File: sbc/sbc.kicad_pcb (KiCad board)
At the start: 4 copper layers, 101.6 x 101.6 mm, 72 parts, among them J1 Controller-Connector, J2 Controller-Connector, J3 SIO-Header, J4 QTPY-RP2040, J5 AVD-Header, J6 AVA-Header, J7 AudioOut-Connector, J8 VideoOut-Connector, J9 Power-Connector, U1 Sally, U10 AT27C256R, U11 AS6C4008-55SIN, U12 TXU0104, U13 TXU0204, U14 AP22814AW5, U2 Antic, U3 GTIA, U4 Pokey, U5 PIA, U6 74AHCT1G125GV,125, U7 74AHCT1G125GV,125, U8 AMU, U9 RMU, X1 3.579545 MHz

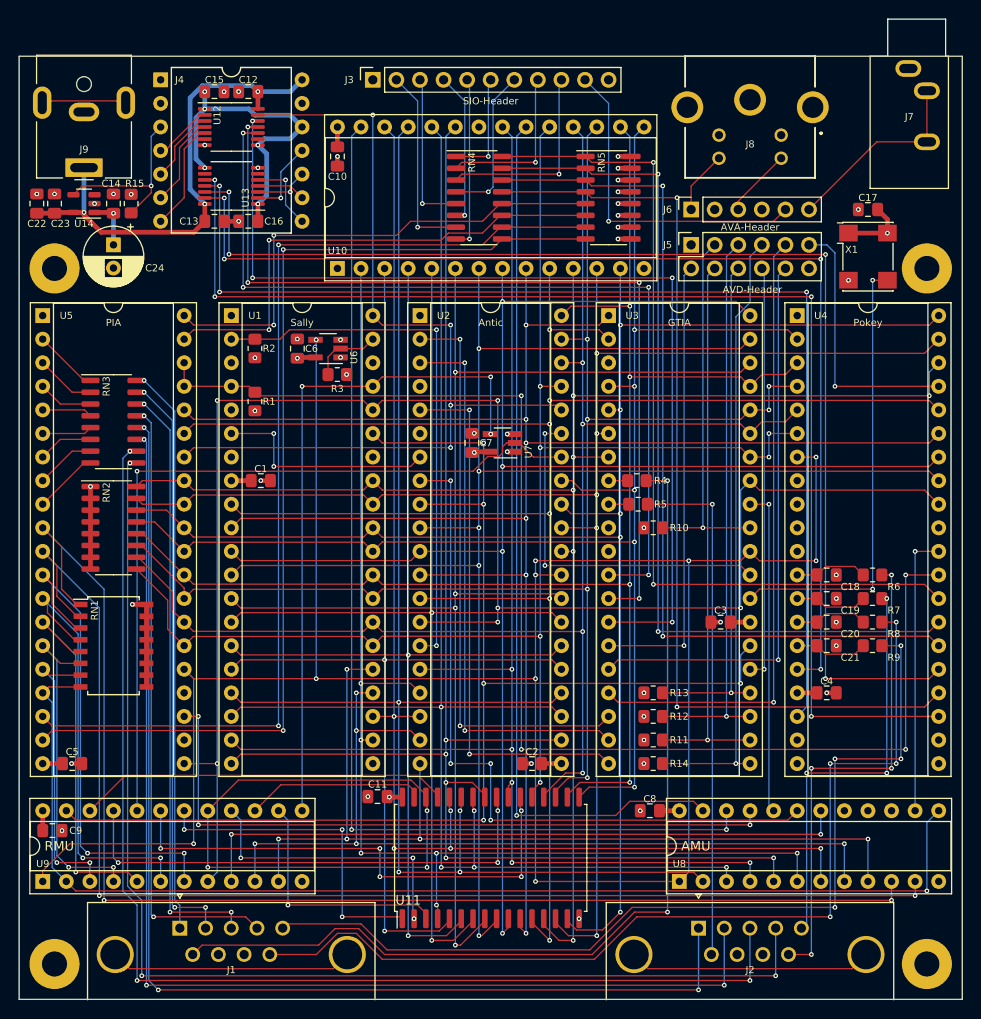
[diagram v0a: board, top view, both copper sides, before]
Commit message: SBC v1.2
SBC fixes/changes:

  - S-Video:
    - Fix S-Video footprint (Y and C swapped, and GNDs swapped) and adapt schematic to match
    - Wire S-Video grounds to AVA header instead of directly to (digital) GND
  - Audio:
    - Wire Audio-Out ground to AVA header
    - Drop SIO audio
    - Pullup open drain pokey audio
  - AMU/RMU:
    - Connect ROM and RAM OE to GND
    - Reserve AMU pin for "IO"
    - Reserve RMU pin for "antic" (registered halt)
    - Support for separate Antic banking (clock RMU with /phi2)
    - Supoprt 130XE and 320XE (compy)
  - Add the option for a resistor between OSC, PHI0 buffer and PHI2 buffer (to reduce over/under-shoot)
  - Invert CA2 (a PNP transistor on the Atari 800 XL inverts this signal)

Additions:

  - SBC Audio/Video board
  - SBC Case
  - SBC SD board

Stylize the complete system as "SFF 320XE".
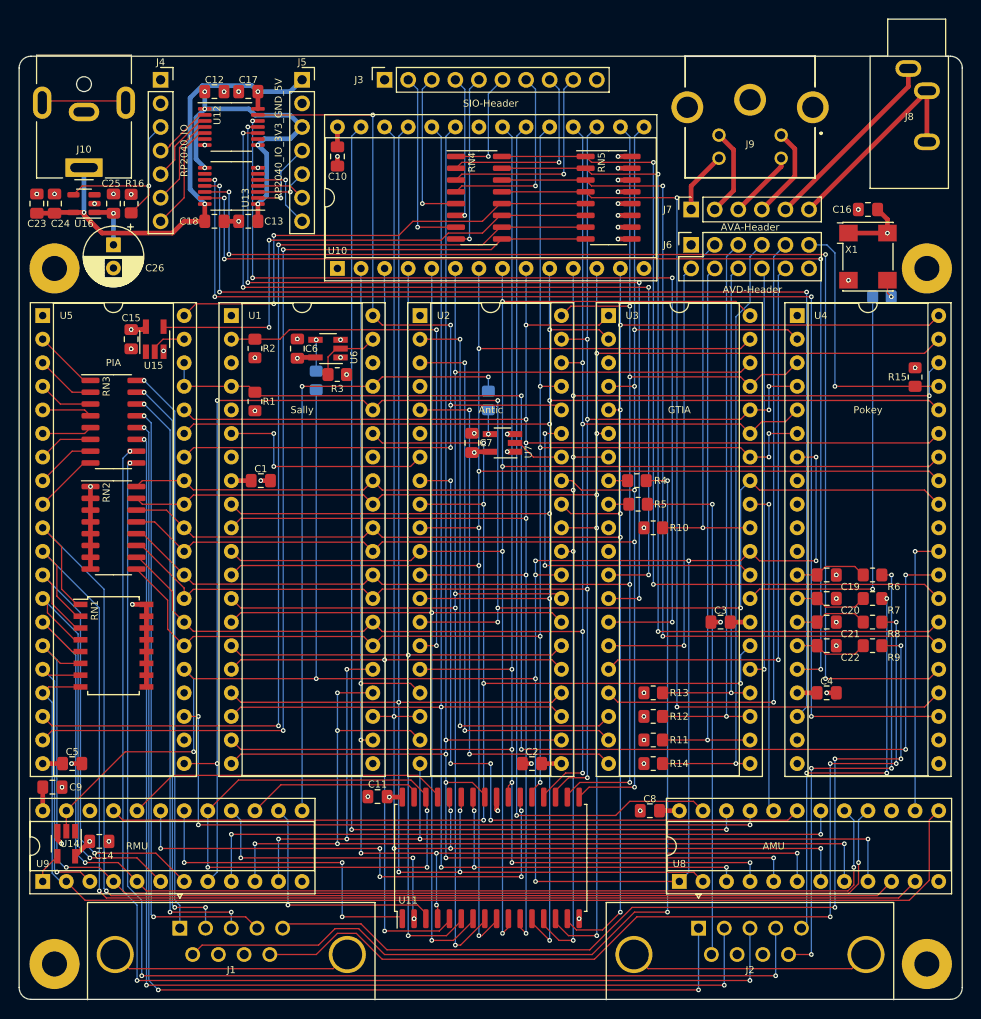
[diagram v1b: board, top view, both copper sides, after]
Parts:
- added C14: 0.1uF, Capacitor_SMD:C_0805_2012Metric_Pad1.18x1.45mm_HandSolder, F.Cu at (110.2, 135.4)
- added C15: 0.1uF, Capacitor_SMD:C_0805_2012Metric_Pad1.18x1.45mm_HandSolder, F.Cu at (113.7, 81.3)
- added J5: RP2040_IO_3V3_GND_5V, Connector_PinSocket_2.54mm:PinSocket_1x07_P2.54mm_Vertical, F.Cu at (132.1, 53.3)
- added R15: 1K, Resistor_SMD:R_0805_2012Metric_Pad1.20x1.40mm_HandSolder, F.Cu at (198.1, 85.4)
- added R17: 0R, Resistor_SMD:R_0805_2012Metric_Pad1.20x1.40mm_HandSolder, B.Cu at (194.5, 76.7)
- added R18: 0R, Resistor_SMD:R_0805_2012Metric_Pad1.20x1.40mm_HandSolder, B.Cu at (152.1, 87.9)
- added R19: 0R, Resistor_SMD:R_0805_2012Metric_Pad1.20x1.40mm_HandSolder, B.Cu at (133.6, 85.7)
- added U14: 74AHCT1G04, Package_TO_SOT_SMD:SOT-23-5_HandSoldering, F.Cu at (106.7, 135.6)
- added U15: 74AHCT1G04, Package_TO_SOT_SMD:SOT-23-5_HandSoldering, F.Cu at (116.2, 81.3)
- J3: footprint Connector_PinSocket_2.54mm:PinSocket_1x11_P2.54mm_Vertical -> Connector_PinSocket_2.54mm:PinSocket_1x10_P2.54mm_Vertical
- J4: value QTPY-RP2040 -> RP2040_IO; footprint Package_DIP:DIP-14_W15.24mm -> Connector_PinSocket_2.54mm:PinSocket_1x07_P2.54mm_Vertical
- moved C9 4.68 mm to (105.2, 129.5)
- moved J3 1.27 mm to (141.0, 53.3)
- renumbered C15 to C12, C16 to C13, C17 to C16, C12 to C17, C13 to C18, C18 to C19, C19 to C20, C20 to C21, C21 to C22, C22 to C23, C23 to C24, C14 to C25, C24 to C26, J9 to J10, J5 to J6, J6 to J7, J7 to J8, J8 to J9, R15 to R16, U14 to U16
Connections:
- net AUDIO_GTIA renamed GTIA_AUDIO
- net AUDIO_POKEY renamed POKEY_AUDIO
- J3 pad 10: AUDIO_SIO -> GND
- J7 pad 1: SVIDEO_C -> SVIDEO_Y
- J7 pad 2: GND -> SVIDEO_Y_GND
- J7 pad 3: SVIDEO_Y -> SVIDEO_C
- J7 pad 4: GND -> SVIDEO_C_GND
- J7 pad 5: AUDIO_SIO -> AUDIO_GND
- J8 pad S: GND -> AUDIO_GND
- J9 pad 1: GND -> SVIDEO_Y_GND
- J9 pad 2: GND -> SVIDEO_C_GND
- RN4 pad 11: CA2 -> Net-(RN4-R6.2)
- RN5 pad 6: CA2 -> Net-(RN4-R6.2)
- U11 pad 24: /OE -> GND
- U2 pad 34: PHI0_UB -> Net-(U2-PHI0)
- U6 pad 4: PHI2 -> Net-(R19-Pad1)
- U7 pad 2: PHI0_UB -> Net-(U2-PHI0)
- U7 pad 4: PHI0 -> Net-(R18-Pad1)
- U8 pad 15: unconnected-(U8-I/O_15-Pad15) -> /memory//io
- U8 pad 16: unconnected-(U8-I/O_16-Pad16) -> PB5
- U8 pad 17: unconnected-(U8-I/O_17-Pad17) -> PB4
- U9 pad 1: PHI2 -> Net-(U9-CLK/IN1)
- U9 pad 20: PHI0_UB -> /WE
- U9 pad 21: /OE -> /HALT
- U9 pad 22: /WE -> /memory//antic
- U9 pad 23: /HALT -> PHI2
- X1 pad 3: Net-(U3-OSC) -> Net-(X1-OUT)
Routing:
- net PB5: track 36.2 -> 125.1 mm
- net PB4: track 40.8 -> 125.9 mm, vias 1 -> 2
- net PHI0_UB: track 84.1 -> 0.00 mm, vias 1 -> 0
- net Net-(RN4-R6.2): track 0.00 -> 55.7 mm, vias 0 -> 2
- net /OE: track 53.6 -> 0.00 mm, vias 3 -> 0
- net CA2: track 54.2 -> 3.54 mm, vias 2 -> 0
- net AUDIO_SIO: track 35.9 -> 0.00 mm, vias 1 -> 0
- net AUDIO_GND: track 0.00 -> 20.7 mm
- net PHI2: track 244.7 -> 229.3 mm, vias 10 -> 9
- net SVIDEO_C_GND: track 0.00 -> 10.1 mm
- net SVIDEO_Y_GND: track 0.00 -> 9.50 mm
- net Net-(U2-PHI0): track 0.00 -> 5.18 mm
- net /HALT: track 137.4 -> 132.3 mm
- net /WE: track 39.9 -> 34.8 mm
- net PHI0: track 72.6 -> 67.7 mm, vias 3 -> 2
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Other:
- outline, holes or cut-outs redrawn
- board text added: "SFF 320XE v1.2 © 2023 Daniel Picken https://github.com/dpicken/atari-hw"
- board text removed: "v1.1 © 2023 Daniel Picken https://github.com/dpicken/atari-hw"

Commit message: SBC v1.3
Motherboard updates:

  - KiCad 9 upgrade
  - USB-C power connector
  - Replace EOL resistor packs with discrete SMD resistors
  - Power/enable voltage translators from switched 5V
  - Fix motor signal pullup
  - Eliminate loop in phi2 traces
  - Thicker clock signal traces

SD card adapter updates:

  - KiCad 9 upgrade
  - Power/enable voltage translator from switched 5V and the eliminate unnecessary SIO pullups

Audio/Video adapter updates:

  - KiCad 9 upgrade
  - No functional changes, gerbers not regenerated, cleaned up bom
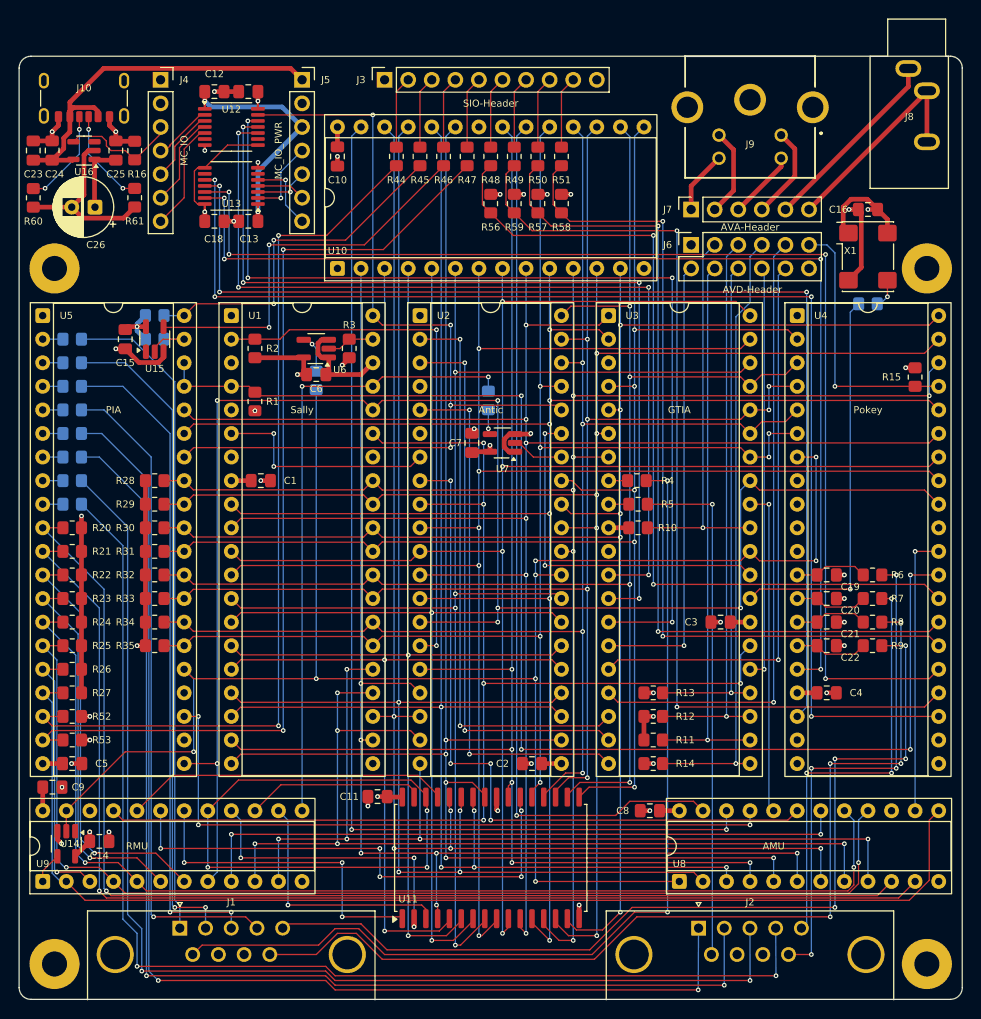
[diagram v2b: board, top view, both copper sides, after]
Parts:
- removed RN1: 3K, Package_SO:SOIC-16W_5.3x10.2mm_P1.27mm
- removed RN2: 10K, Package_SO:SOIC-16_3.9x9.9mm_P1.27mm
- removed RN3: 220R, Package_SO:SOIC-16_3.9x9.9mm_P1.27mm
- removed RN4: 100R, Package_SO:SOIC-16_3.9x9.9mm_P1.27mm
- removed RN5: 4.7K, Package_SO:SOIC-16_3.9x9.9mm_P1.27mm
- added R20: 3K, Resistor_SMD:R_0805_2012Metric_Pad1.20x1.40mm_HandSolder, F.Cu at (107.3, 101.6)
- added R21: 3K, Resistor_SMD:R_0805_2012Metric_Pad1.20x1.40mm_HandSolder, F.Cu at (107.3, 104.1)
- added R22: 3K, Resistor_SMD:R_0805_2012Metric_Pad1.20x1.40mm_HandSolder, F.Cu at (107.3, 106.7)
- added R23: 3K, Resistor_SMD:R_0805_2012Metric_Pad1.20x1.40mm_HandSolder, F.Cu at (107.3, 109.2)
- added R24: 3K, Resistor_SMD:R_0805_2012Metric_Pad1.20x1.40mm_HandSolder, F.Cu at (107.3, 111.8)
- added R25: 3K, Resistor_SMD:R_0805_2012Metric_Pad1.20x1.40mm_HandSolder, F.Cu at (107.3, 114.3)
- added R26: 3K, Resistor_SMD:R_0805_2012Metric_Pad1.20x1.40mm_HandSolder, F.Cu at (107.3, 116.8)
- added R27: 3K, Resistor_SMD:R_0805_2012Metric_Pad1.20x1.40mm_HandSolder, F.Cu at (107.3, 119.4)
- added R28: 10K, Resistor_SMD:R_0805_2012Metric_Pad1.20x1.40mm_HandSolder, F.Cu at (116.2, 96.5)
- added R29: 10K, Resistor_SMD:R_0805_2012Metric_Pad1.20x1.40mm_HandSolder, F.Cu at (116.2, 99.1)
- added R30: 10K, Resistor_SMD:R_0805_2012Metric_Pad1.20x1.40mm_HandSolder, F.Cu at (116.2, 101.6)
- added R31: 10K, Resistor_SMD:R_0805_2012Metric_Pad1.20x1.40mm_HandSolder, F.Cu at (116.2, 104.1)
- added R32: 10K, Resistor_SMD:R_0805_2012Metric_Pad1.20x1.40mm_HandSolder, F.Cu at (116.2, 106.7)
- added R33: 10K, Resistor_SMD:R_0805_2012Metric_Pad1.20x1.40mm_HandSolder, F.Cu at (116.2, 109.2)
- added R34: 10K, Resistor_SMD:R_0805_2012Metric_Pad1.20x1.40mm_HandSolder, F.Cu at (116.2, 111.8)
- added R35: 10K, Resistor_SMD:R_0805_2012Metric_Pad1.20x1.40mm_HandSolder, F.Cu at (116.2, 114.3)
- added R36: 220R, Resistor_SMD:R_0805_2012Metric_Pad1.20x1.40mm_HandSolder, B.Cu at (107.3, 81.3)
- added R37: 220R, Resistor_SMD:R_0805_2012Metric_Pad1.20x1.40mm_HandSolder, B.Cu at (107.3, 83.8)
- added R38: 220R, Resistor_SMD:R_0805_2012Metric_Pad1.20x1.40mm_HandSolder, B.Cu at (107.3, 86.4)
- added R39: 220R, Resistor_SMD:R_0805_2012Metric_Pad1.20x1.40mm_HandSolder, B.Cu at (107.3, 88.9)
- added R40: 220R, Resistor_SMD:R_0805_2012Metric_Pad1.20x1.40mm_HandSolder, B.Cu at (107.3, 91.4)
- added R41: 220R, Resistor_SMD:R_0805_2012Metric_Pad1.20x1.40mm_HandSolder, B.Cu at (107.3, 94.0)
- added R42: 220R, Resistor_SMD:R_0805_2012Metric_Pad1.20x1.40mm_HandSolder, B.Cu at (107.3, 96.5)
- added R43: 220R, Resistor_SMD:R_0805_2012Metric_Pad1.20x1.40mm_HandSolder, B.Cu at (107.3, 99.1)
- added R44: 100R, Resistor_SMD:R_0805_2012Metric_Pad1.20x1.40mm_HandSolder, F.Cu at (142.2, 61.6)
- added R45: 100R, Resistor_SMD:R_0805_2012Metric_Pad1.20x1.40mm_HandSolder, F.Cu at (144.8, 61.6)
- added R46: 100R, Resistor_SMD:R_0805_2012Metric_Pad1.20x1.40mm_HandSolder, F.Cu at (147.3, 61.6)
- added R47: 100R, Resistor_SMD:R_0805_2012Metric_Pad1.20x1.40mm_HandSolder, F.Cu at (149.9, 61.6)
- added R48: 100R, Resistor_SMD:R_0805_2012Metric_Pad1.20x1.40mm_HandSolder, F.Cu at (152.4, 61.6)
- added R49: 100R, Resistor_SMD:R_0805_2012Metric_Pad1.20x1.40mm_HandSolder, F.Cu at (154.9, 61.6)
- added R50: 100R, Resistor_SMD:R_0805_2012Metric_Pad1.20x1.40mm_HandSolder, F.Cu at (157.5, 61.6)
- added R51: 100R, Resistor_SMD:R_0805_2012Metric_Pad1.20x1.40mm_HandSolder, F.Cu at (160.0, 61.6)
- added R52: 4.7K, Resistor_SMD:R_0805_2012Metric_Pad1.20x1.40mm_HandSolder, F.Cu at (107.3, 121.9)
- added R53: 4.7K, Resistor_SMD:R_0805_2012Metric_Pad1.20x1.40mm_HandSolder, F.Cu at (107.3, 124.5)
- added R54: 4.7K, Resistor_SMD:R_0805_2012Metric_Pad1.20x1.40mm_HandSolder, B.Cu at (116.2, 78.7)
- added R55: 4.7K, Resistor_SMD:R_0805_2012Metric_Pad1.20x1.40mm_HandSolder, B.Cu at (116.2, 81.3)
- added R56: 4.7K, Resistor_SMD:R_0805_2012Metric_Pad1.20x1.40mm_HandSolder, F.Cu at (152.4, 66.7)
- added R57: 4.7K, Resistor_SMD:R_0805_2012Metric_Pad1.20x1.40mm_HandSolder, F.Cu at (157.5, 66.7)
- added R58: 4.7K, Resistor_SMD:R_0805_2012Metric_Pad1.20x1.40mm_HandSolder, F.Cu at (160.0, 66.7)
- added R59: 4.7K, Resistor_SMD:R_0805_2012Metric_Pad1.20x1.40mm_HandSolder, F.Cu at (154.9, 66.7)
- added R60: 5.1K, Resistor_SMD:R_0805_2012Metric_Pad1.20x1.40mm_HandSolder, F.Cu at (103.1, 66.1)
- added R61: 5.1K, Resistor_SMD:R_0805_2012Metric_Pad1.20x1.40mm_HandSolder, F.Cu at (114.0, 66.0)
- J1, J2: value Controller-Connector -> DE9_Pins_MountingHoles; footprint Project_Connector_Dsub:DSUB-9_Male_Horizontal_PDI-09S-5-RG30 -> Connector_Dsub:DSUB-9_Pins_Horizontal_P2.77x2.84mm_EdgePinOffset4.94mm_Housed_MountingHolesOffset4.94mm
- J10: value Power-Connector -> USB_C_Receptacle_PowerOnly_6P; footprint Connector_BarrelJack:BarrelJack_CUI_PJ-063AH_Horizontal -> Connector_USB:USB_C_Receptacle_GCT_USB4125-xx-x_6P_TopMnt_Horizontal
- J4: value RP2040_IO -> MC_IO
- J5: value RP2040_IO_3V3_GND_5V -> MC_IO_PWR
- R17, R18, R19: value 0R -> 33R
- U11: footprint Package_SO:SSOP-32_11.305x20.495mm_P1.27mm -> Package_SO:SOP-32_11.305x20.495mm_P1.27mm
- moved J10 8.57 mm to (108.6, 54.2)
- moved C23 5.73 mm to (103.1, 61.0)
- moved R16 5.73 mm to (114.0, 61.0)
- moved C24 5.72 mm to (105.2, 61.0)
- moved C25 5.72 mm to (112.0, 61.0)
- moved U16 5.71 mm to (108.6, 61.0)
- moved C26 4.53 mm to (109.8, 67.1), turned to 180 degrees
- moved C6 3.45 mm to (133.6, 85.1), turned to 0 degrees
- moved R3 3.09 mm to (137.2, 82.3), turned to -90 degrees
- moved R17 1.69 mm to (193.0, 77.5)
- moved R10 1.63 mm to (168.3, 101.6)
- moved U6 1.27 mm to (133.6, 82.3)
- moved C15 0.64 mm to (113.0, 81.3)
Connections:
- C12 pad 1: +3.3V -> +3.3VP
- C13 pad 1: +3.3V -> +3.3VP
- C17 pad 1: +5VP -> +5V
- C18 pad 1: +5VP -> +5V
- J5 pad 3: +3.3V -> +3.3VP
- U12 pad 1: +3.3V -> +3.3VP
- U12 pad 14: +5VP -> +5V
- U12 pad 8: +3.3V -> +5V
- U13 pad 1: +3.3V -> +3.3VP
- U13 pad 14: +5VP -> +5V
- U13 pad 8: +3.3V -> +5V
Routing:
- net GND: track 12.5 -> 85.1 mm, vias 37 -> 27
- net +5V: track 70.1 -> 128.8 mm, vias 26 -> 22
- net PHI2: track 229.3 -> 194.4 mm, vias 9 -> 8
- net +3.3V: track 34.8 -> 0.00 mm, vias 5 -> 0
- net +3.3VP: track 0.00 -> 26.5 mm, vias 0 -> 2
- net unconnected-(J2-PAD-Pad0): track 26.3 -> 0.00 mm
- net unconnected-(J1-PAD-Pad0): track 26.3 -> 0.00 mm
- net CB1: track 111.3 -> 96.6 mm
- net SIO_CLOCK_IN: track 22.5 -> 7.78 mm, vias 1 -> 0
- net CA1: track 52.4 -> 38.3 mm
- net Net-(R46-Pad1): track 55.7 -> 42.5 mm
- net SIO_DATA_IN: track 20.7 -> 7.78 mm, vias 1 -> 0
- net SIO_CLOCK_OUT: track 20.7 -> 7.78 mm, vias 1 -> 0
- net SIO_IRQ: track 20.4 -> 7.78 mm, vias 1 -> 0
- net SIO_COMMAND: track 19.0 -> 7.78 mm, vias 1 -> 0
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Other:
- board text added: "SFF 320XE v1.3 © 2026 Daniel Picken https://github.com/dpicken/atari-hw"
- board text removed: "SFF 320XE v1.2 © 2023 Daniel Picken https://github.com/dpicken/atari-hw"
